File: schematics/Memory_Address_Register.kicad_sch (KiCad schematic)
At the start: 27 parts, among them SW1 SW_DIP_x08, SW2 SW_SPDT, U1 74LS173, U2 74LS173, U3 74LS157, U4 74LS157

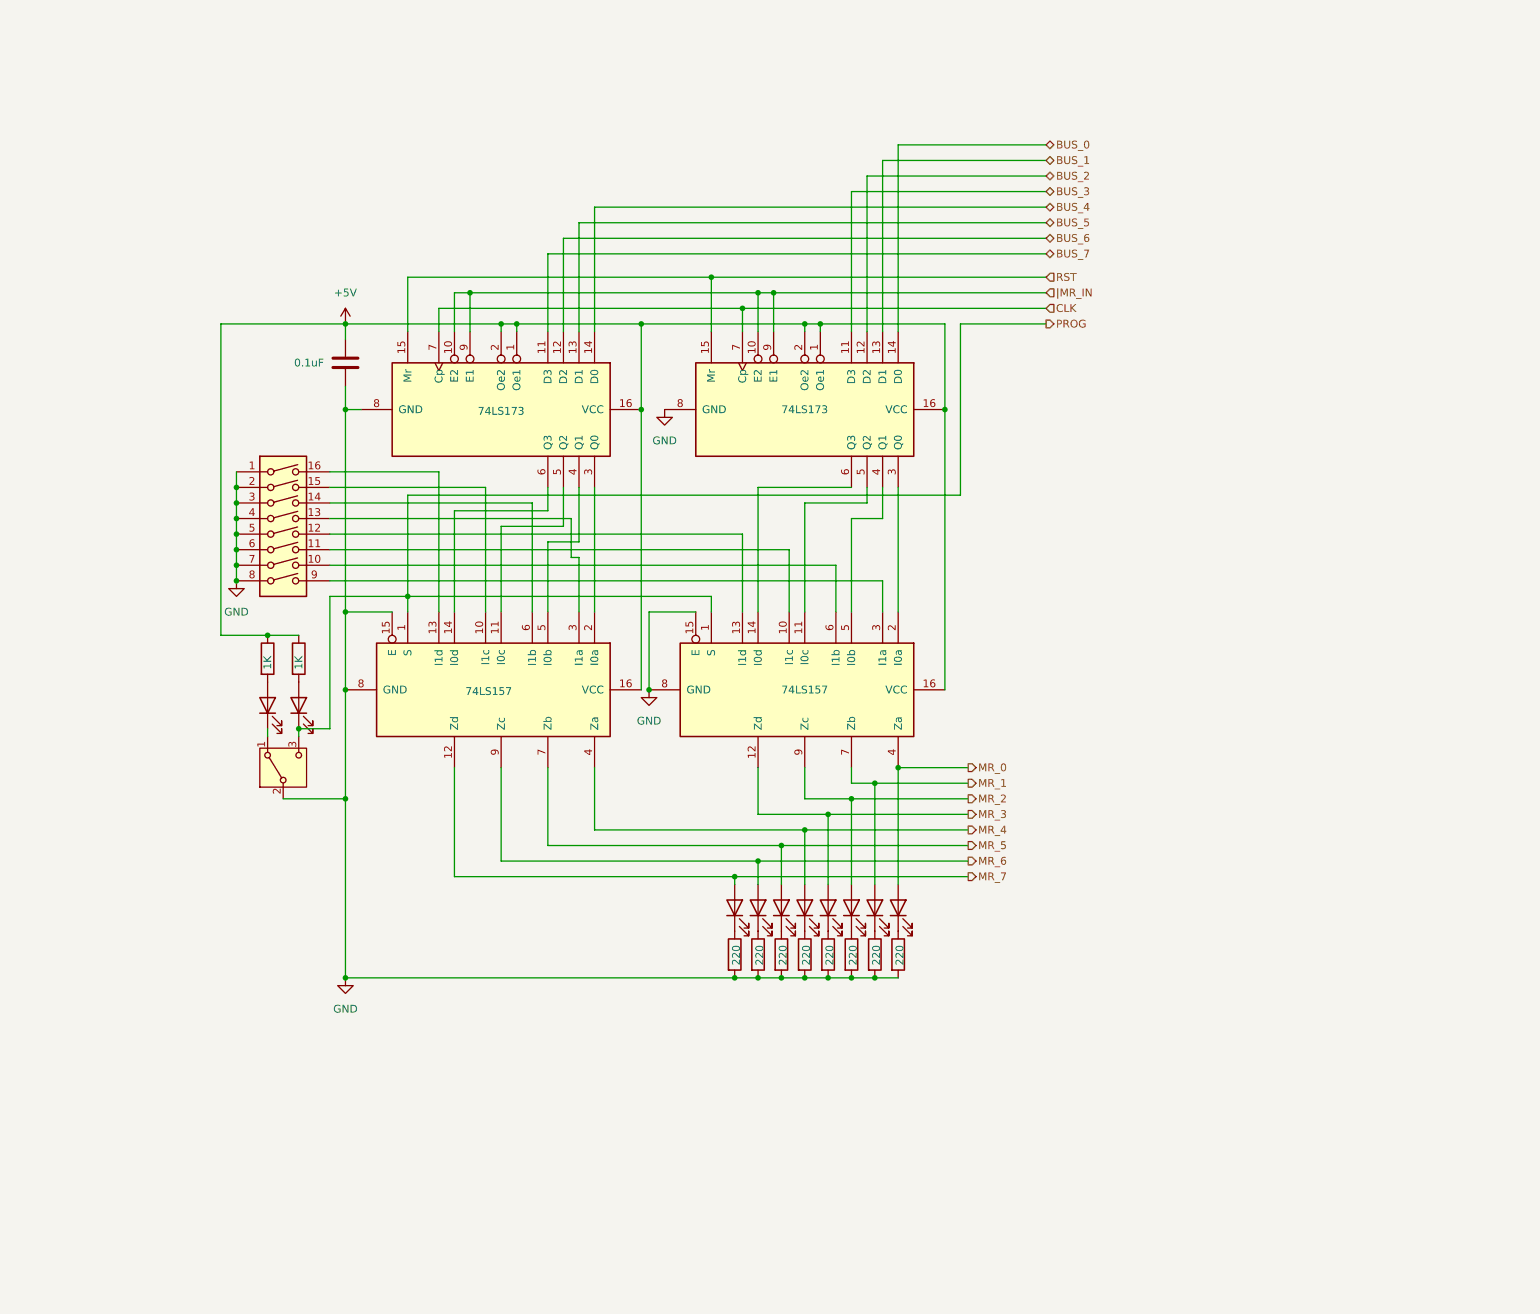
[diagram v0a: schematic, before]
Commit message: feat: updated electrical diagrams & individual part list
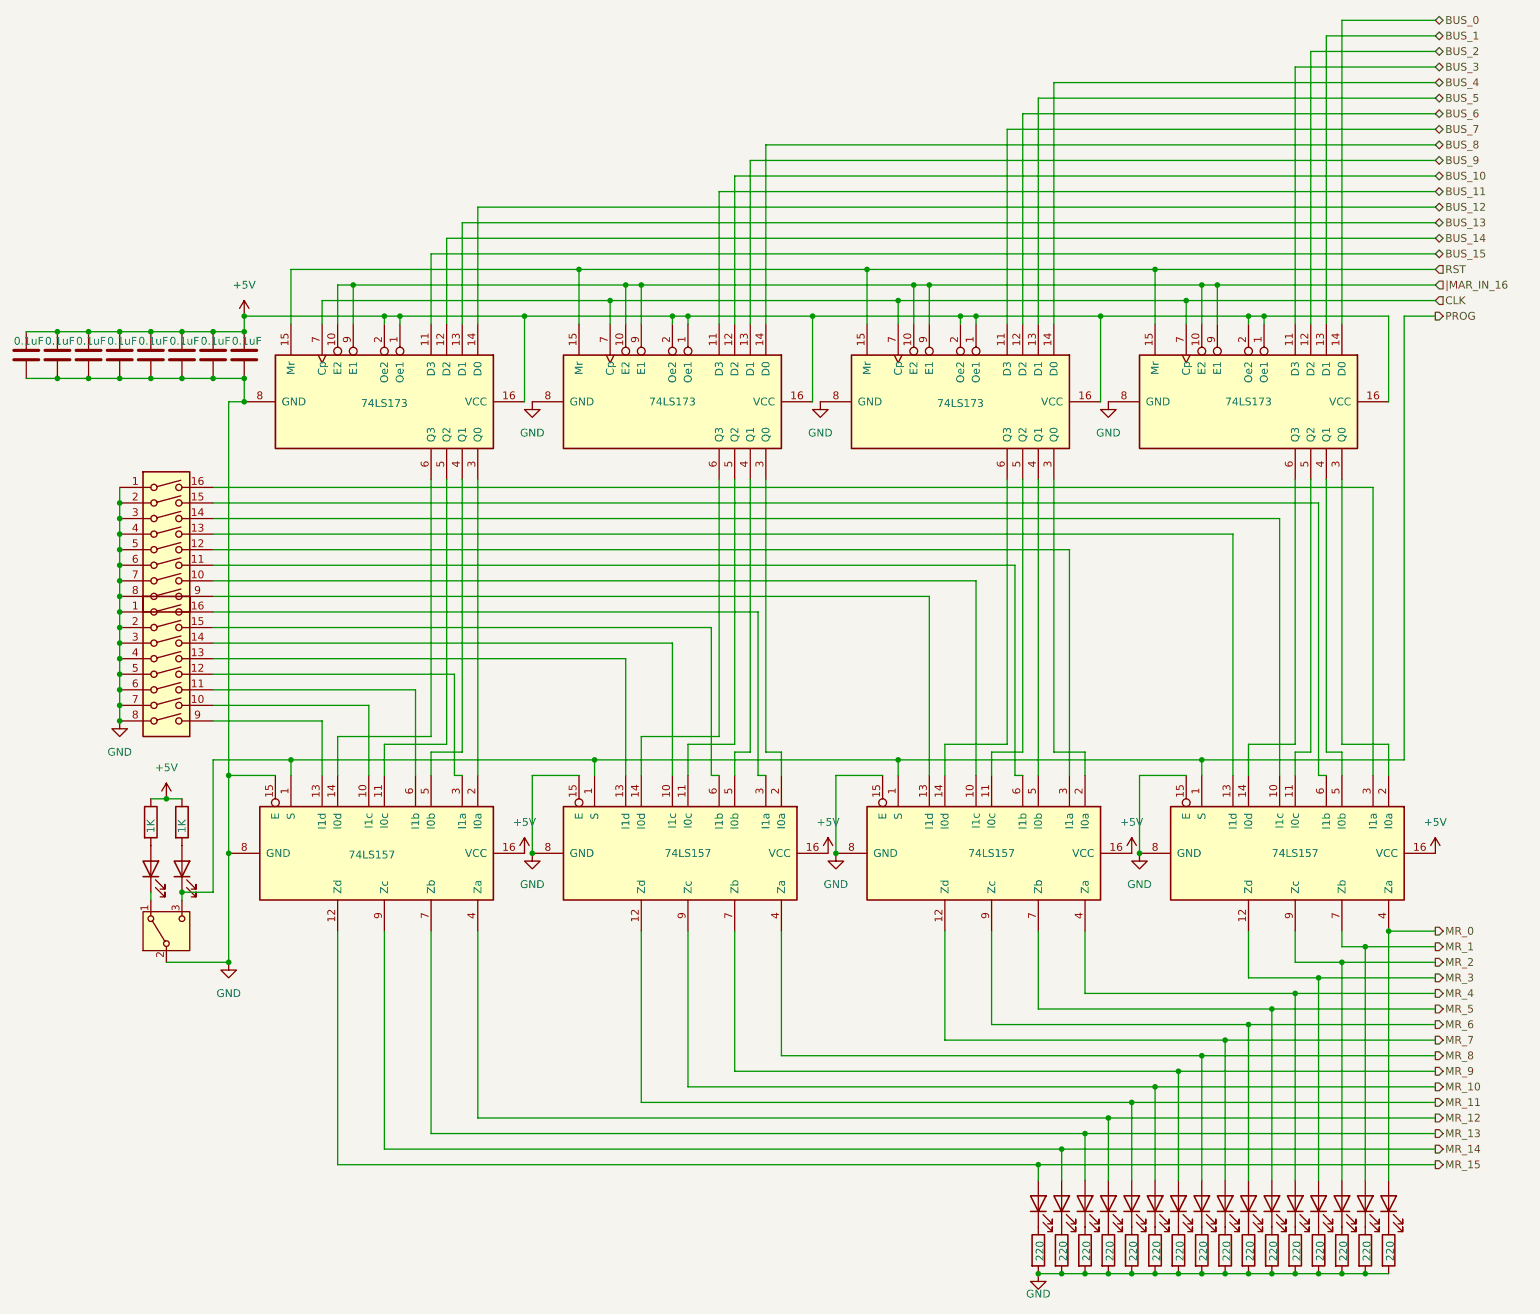
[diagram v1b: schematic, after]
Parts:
- added C2, C3, C4, C5, C6, C7, C8: 0.1uF, symbol Device:C
- added D11, D12, D13, D14, D15, D16, D17, D18: LED, symbol Device:LED
- added R11, R12, R13, R14, R15, R16, R17, R18: 220, symbol Device:R
- added SW3: SW_DIP_x08, symbol Switch:SW_DIP_x08
- added U5, U6: 74LS173, symbol 74xx:74LS173
- added U7, U8: 74LS157, symbol 74xx:74LS157
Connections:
- net +5V: now also C2.1, C3.1, C4.1, C5.1, C6.1, C7.1, C8.1, U5.1 (Oe1), U5.16 (VCC), U5.2 (Oe2), U6.1 (Oe1), U6.16 (VCC), U6.2 (Oe2), U7.16 (VCC), U8.16 (VCC)
- net BUS_0: now also U6.14 (D0); no longer U2.14 (D0)
- net BUS_1: now also U6.13 (D1); no longer U2.13 (D1)
- net BUS_2: now also U6.12 (D2); no longer U2.12 (D2)
- net BUS_3: now also U6.11 (D3); no longer U2.11 (D3)
- net BUS_4: now also U5.14 (D0); no longer U1.14 (D0)
- net BUS_5: now also U5.13 (D1); no longer U1.13 (D1)
- net BUS_6: now also U5.12 (D2); no longer U1.12 (D2)
- net BUS_7: now also U5.11 (D3); no longer U1.11 (D3)
- net CLK: now also U5.7 (Cp), U6.7 (Cp)
- net GND: now also C2.2, C3.2, C4.2, C5.2, C6.2, C7.2, C8.2, R11.2, R12.2, R13.2, R14.2, R15.2, R16.2, R17.2, R18.2, SW3.1, SW3.2, SW3.3, SW3.4, SW3.5, SW3.6, SW3.7, SW3.8, U5.8 (GND), U6.8 (GND), U7.15 (E), U7.8 (GND), U8.15 (E), U8.8 (GND)
- net MR_0: now also D18.2 (A), U8.4 (Za); no longer D8.2 (A), U3.4 (Za)
- net MR_1: now also D17.2 (A), U8.7 (Zb); no longer D7.2 (A), U3.7 (Zb)
- net MR_2: now also D16.2 (A), U8.9 (Zc); no longer D6.2 (A), U3.9 (Zc)
- net MR_3: now also D15.2 (A), U8.12 (Zd); no longer D5.2 (A), U3.12 (Zd)
- net MR_4: now also D14.2 (A), U7.4 (Za); no longer D4.2 (A), U4.4 (Za)
- net MR_5: now also D13.2 (A), U7.7 (Zb); no longer D3.2 (A), U4.7 (Zb)
- net MR_6: now also D12.2 (A), U7.9 (Zc); no longer D2.2 (A), U4.9 (Zc)
- net MR_7: now also D11.2 (A), U7.12 (Zd); no longer D1.2 (A), U4.12 (Zd)
- net PROG: now also U7.1 (S), U8.1 (S)
- net RST: now also U5.15 (Mr), U6.15 (Mr)
- net at SW1.10: now also U4.10 (I1c); no longer U3.6 (I1b)
- net at SW1.11: now also U4.6 (I1b); no longer U3.10 (I1c)
- net at SW1.12: now also U4.3 (I1a); no longer U3.13 (I1d)
- net at SW1.13: now also U3.13 (I1d); no longer U4.3 (I1a)
- net at SW1.14: now also U3.10 (I1c); no longer U4.6 (I1b)
- net at SW1.15: now also U3.6 (I1b); no longer U4.10 (I1c)
- net at SW1.16: now also U3.3 (I1a); no longer U4.13 (I1d)
- net at SW1.9: now also U4.13 (I1d); no longer U3.3 (I1a)
- net |MR_IN renamed |MAR_IN_16
- net |MAR_IN_16: now also U5.10 (E2), U5.9 (E1), U6.10 (E2), U6.9 (E1)
- new net: SW3.10, U7.10 (I1c)
- new net: SW3.11, U7.6 (I1b)
- new net: SW3.12, U7.3 (I1a)
- new net: SW3.13, U8.13 (I1d)
- new net: SW3.14, U8.10 (I1c)
- new net: SW3.15, U8.6 (I1b)
- new net: SW3.16, U8.3 (I1a)
- new net: SW3.9, U7.13 (I1d)
- new net: D15.1 (K), R15.1
- new net: D14.1 (K), R14.1
- new net: U5.3 (Q0), U7.2 (I0a)
- new net: U5.4 (Q1), U7.5 (I0b)
- new net: U5.5 (Q2), U7.11 (I0c)
- new net: U5.6 (Q3), U7.14 (I0d)
- new net: U6.3 (Q0), U8.2 (I0a)
- new net: U6.4 (Q1), U8.5 (I0b)
- new net: U6.5 (Q2), U8.11 (I0c)
- new net: U6.6 (Q3), U8.14 (I0d)
- new net: D16.1 (K), R16.1
- new net: D17.1 (K), R17.1
- new net: D12.1 (K), R12.1
- new net: D18.1 (K), R18.1
- new net: D13.1 (K), R13.1
- new net: D11.1 (K), R11.1
- new net BUS_10: U2.12 (D2)
- new net BUS_11: U2.11 (D3)
- new net BUS_12: U1.14 (D0)
- new net BUS_13: U1.13 (D1)
- new net BUS_14: U1.12 (D2)
- new net BUS_15: U1.11 (D3)
- new net BUS_8: U2.14 (D0)
- new net BUS_9: U2.13 (D1)
- new net MR_10: D6.2 (A), U3.9 (Zc)
- new net MR_11: D5.2 (A), U3.12 (Zd)
- new net MR_12: D4.2 (A), U4.4 (Za)
- new net MR_13: D3.2 (A), U4.7 (Zb)
- new net MR_14: D2.2 (A), U4.9 (Zc)
- new net MR_15: D1.2 (A), U4.12 (Zd)
- new net MR_8: D8.2 (A), U3.4 (Za)
- new net MR_9: D7.2 (A), U3.7 (Zb)

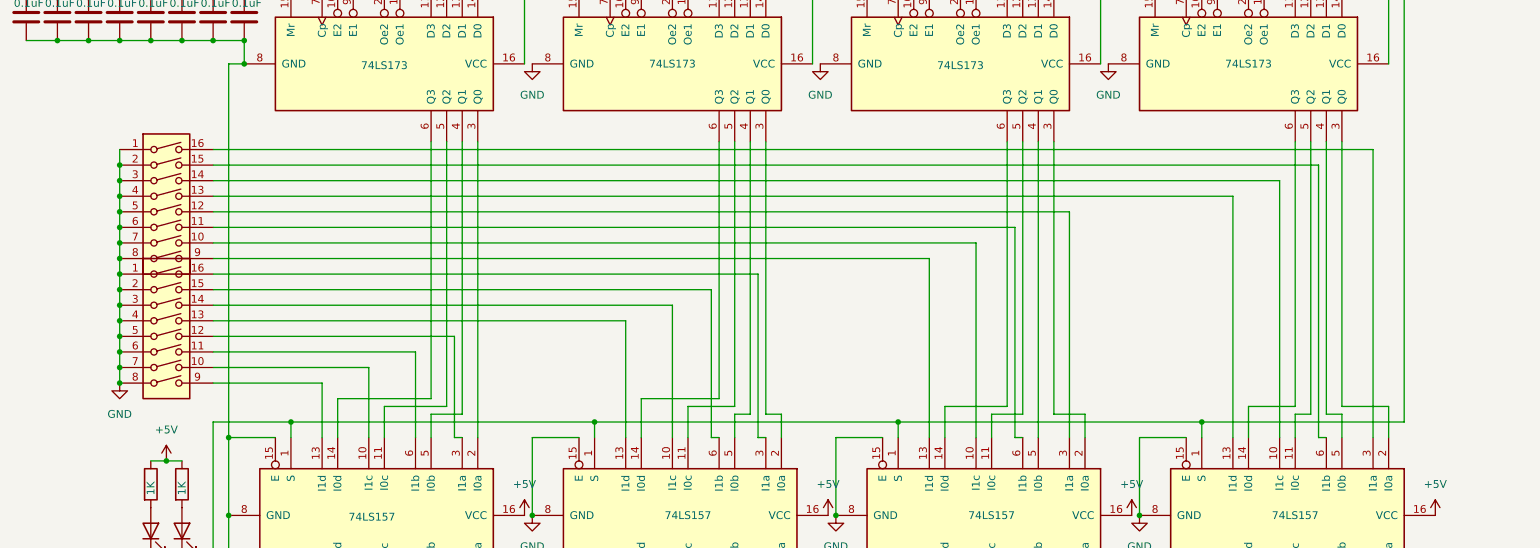
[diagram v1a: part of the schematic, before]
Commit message: Updated schematics and README
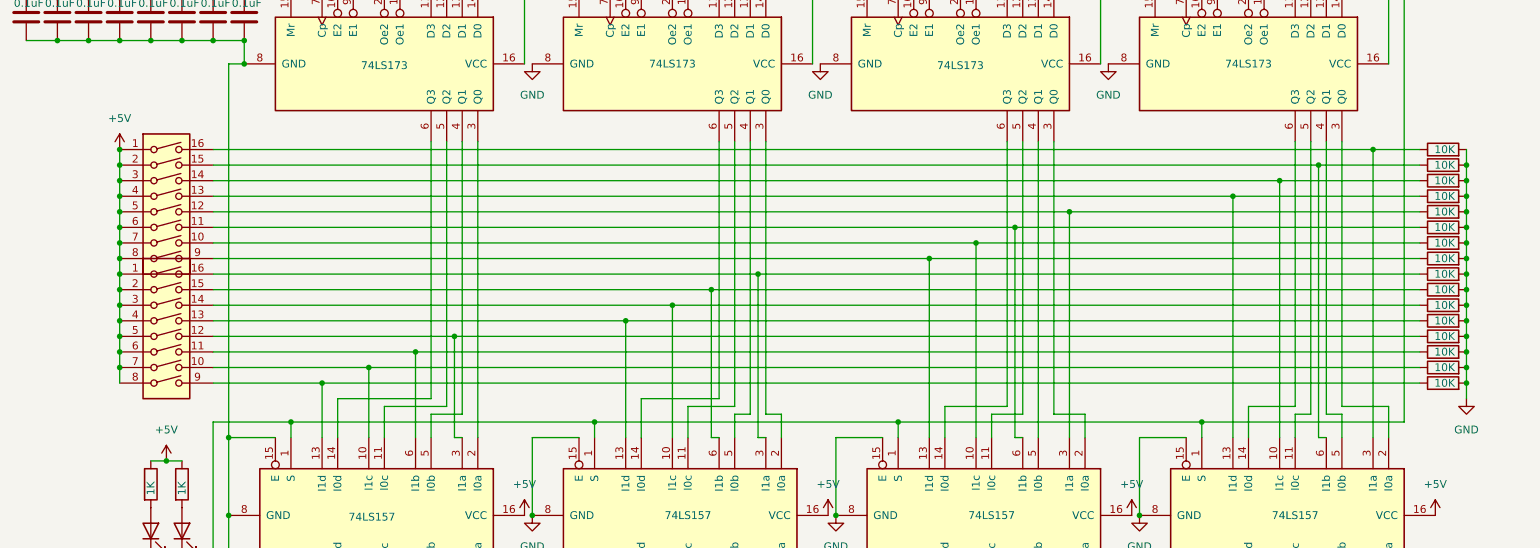
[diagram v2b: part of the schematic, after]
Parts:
- added R19, R20, R21, R22, R23, R24, R25, R26, R27, R28, R29, R30, R31, R32, R33, R34: 10K, symbol Device:R
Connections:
- net +5V: now also SW1.1, SW1.2, SW1.3, SW1.4, SW1.5, SW1.6, SW1.7, SW1.8, SW3.1, SW3.2, SW3.3, SW3.4, SW3.5, SW3.6, SW3.7, SW3.8
- net GND: now also R19.2, R20.2, R21.2, R22.2, R23.2, R24.2, R25.2, R26.2, R27.2, R28.2, R29.2, R30.2, R31.2, R32.2, R33.2, R34.2; no longer SW1.1, SW1.2, SW1.3, SW1.4, SW1.5, SW1.6, SW1.7, SW1.8, SW3.1, SW3.2, SW3.3, SW3.4, SW3.5, SW3.6, SW3.7, SW3.8
- net at SW3.10, U7.10 (I1c): now also R25.1
- net at SW3.11, U7.6 (I1b): now also R24.1
- net at SW3.12, U7.3 (I1a): now also R23.1
- net at SW3.13, U8.13 (I1d): now also R22.1
- net at SW3.14, U8.10 (I1c): now also R21.1
- net at SW3.15, U8.6 (I1b): now also R20.1
- net at SW3.16, U8.3 (I1a): now also R19.1
- net at SW3.9, U7.13 (I1d): now also R26.1
- net at SW1.10, U4.10 (I1c): now also R33.1
- net at SW1.11, U4.6 (I1b): now also R32.1
- net at SW1.12, U4.3 (I1a): now also R31.1
- net at SW1.13, U3.13 (I1d): now also R30.1
- net at SW1.14, U3.10 (I1c): now also R29.1
- net at SW1.15, U3.6 (I1b): now also R28.1
- net at SW1.16, U3.3 (I1a): now also R27.1
- net at SW1.9, U4.13 (I1d): now also R34.1
